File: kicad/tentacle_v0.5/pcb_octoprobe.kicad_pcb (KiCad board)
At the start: 2 copper layers, 100 x 165 mm, 736 parts, among them J101 USB-226-BRW, J1302 Conn_02x20, J1303 Conn_02x20, J1501 Conn_02x20, J1502 Conn_01x12, J201 Conn_02x05, J301 USB_C_Receptacle_USB2.0, J501 Conn_02x20, U1001 GAQY221S, U1101 GAQY221S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

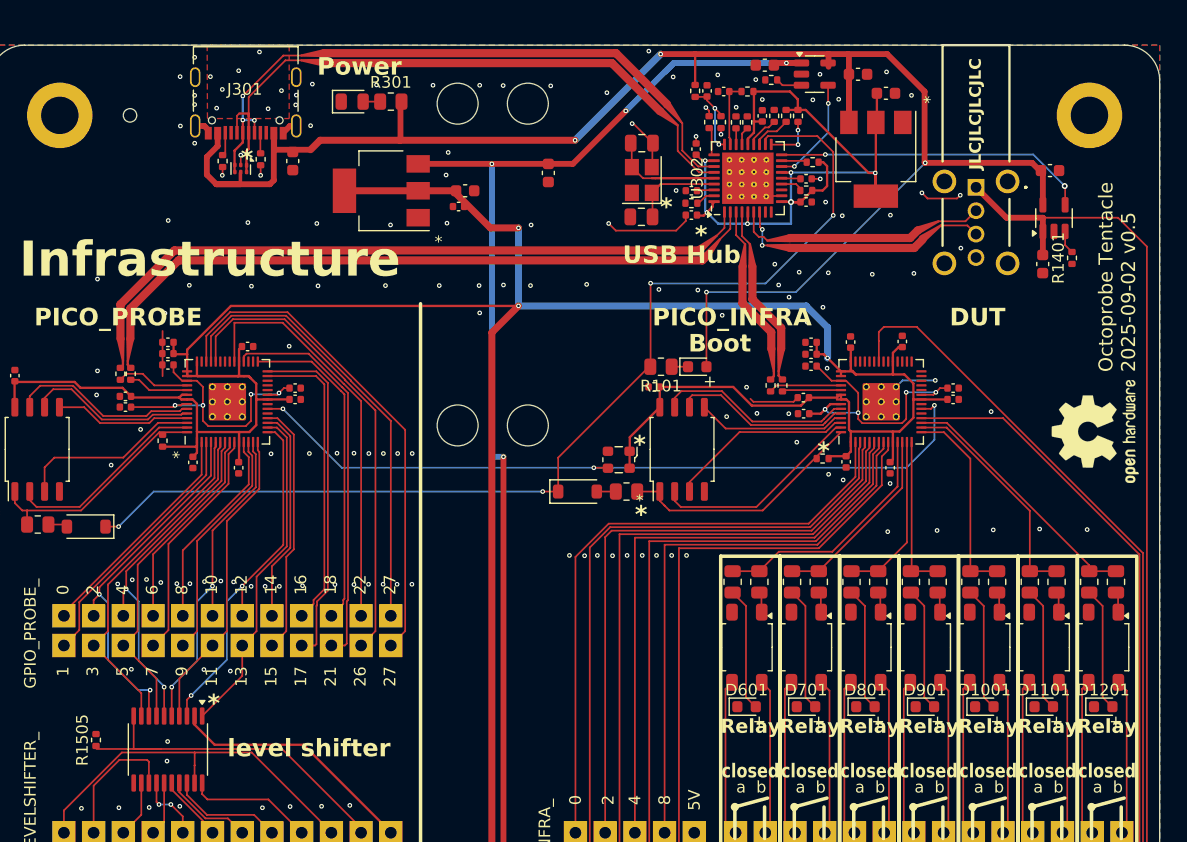
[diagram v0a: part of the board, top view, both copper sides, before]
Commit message: Kicad 9.04. Remove silkscreen: R301, U302, R1401, R1505
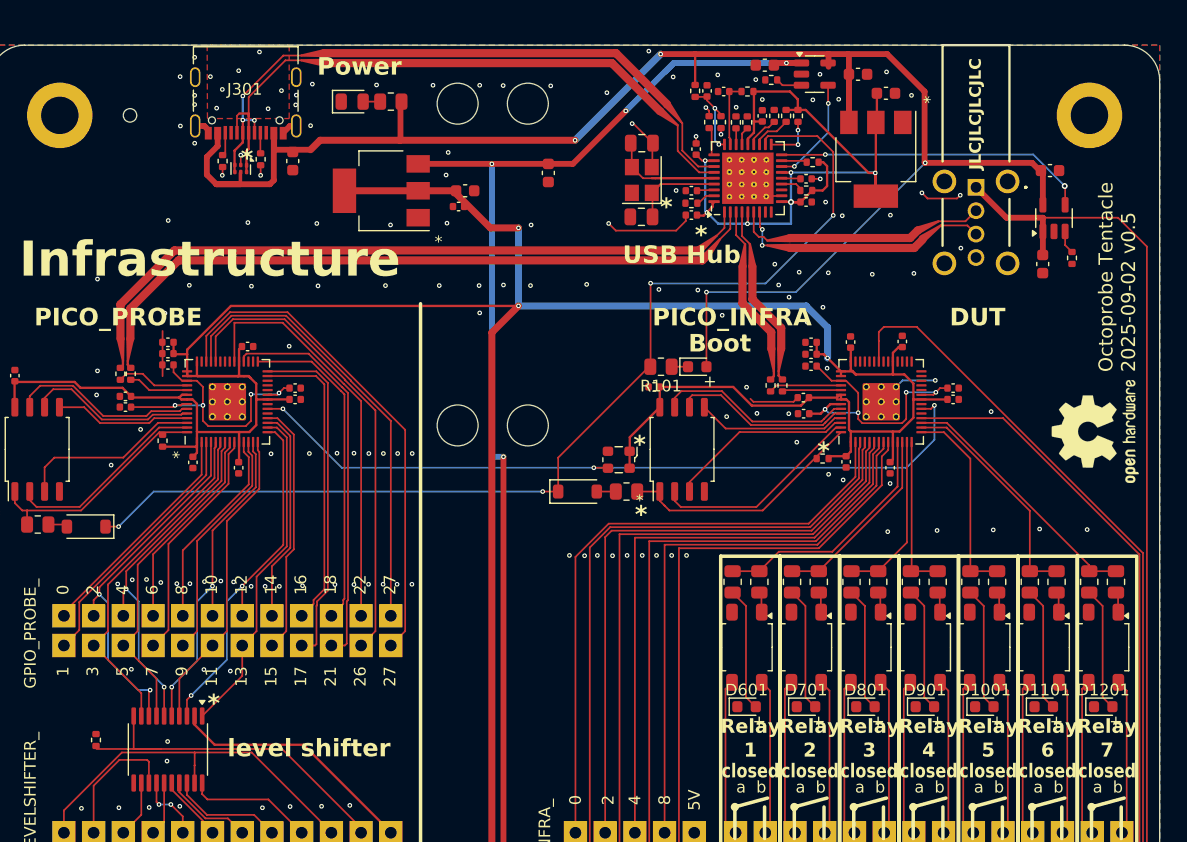
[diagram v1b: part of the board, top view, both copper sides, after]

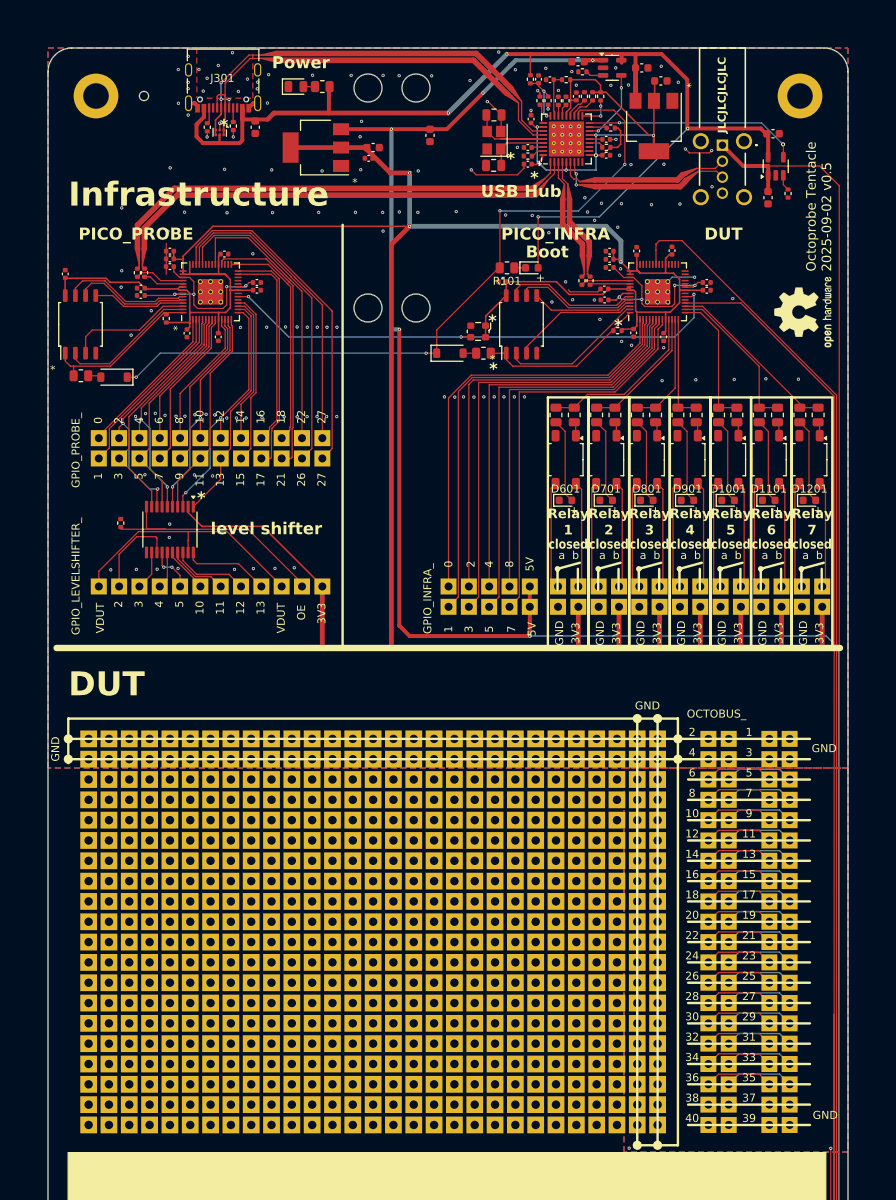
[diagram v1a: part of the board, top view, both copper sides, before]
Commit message: Breadbord pads: Only one ground line to leave more space for DUT-boards
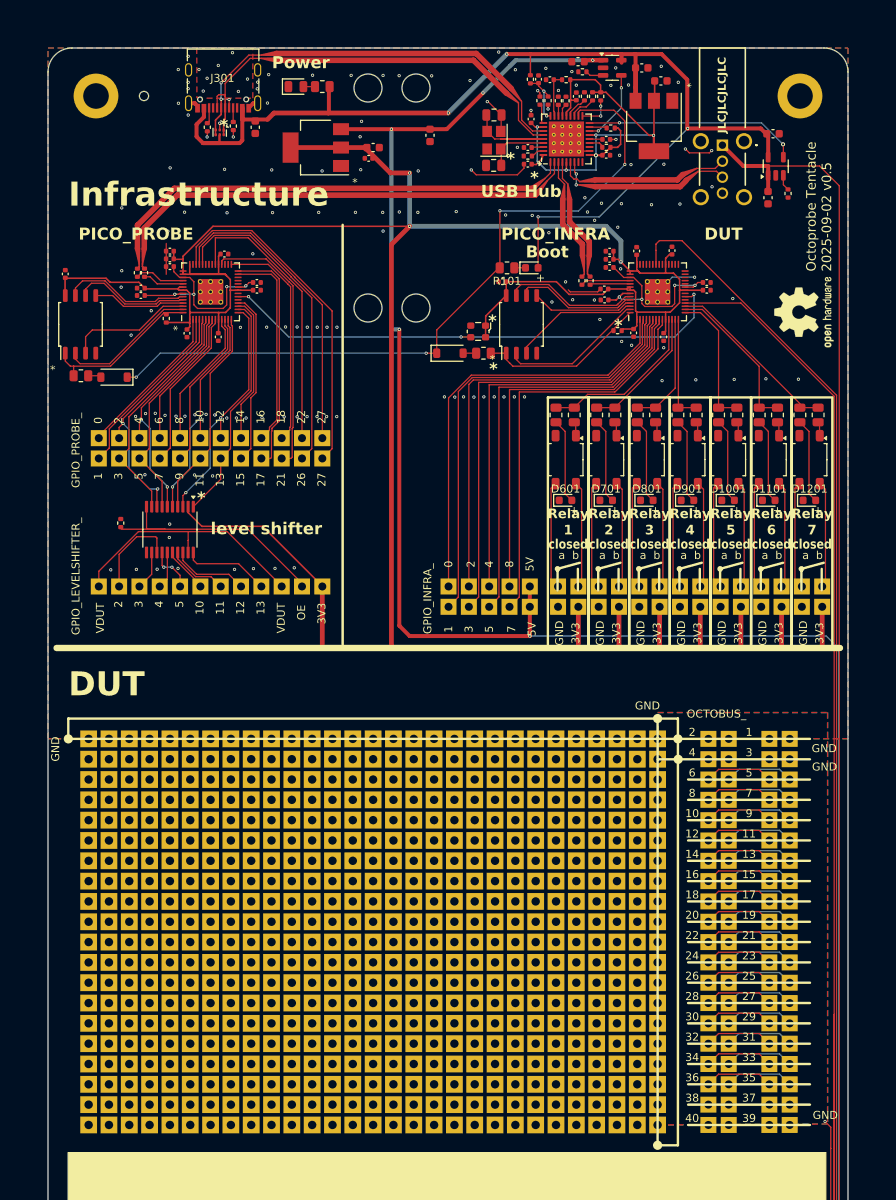
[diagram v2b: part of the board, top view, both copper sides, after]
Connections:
- BP1301 pad 1: GND -> (no net) (x46)
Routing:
- net GND: track 188.6 -> 192.2 mm, vias 155 -> 154
